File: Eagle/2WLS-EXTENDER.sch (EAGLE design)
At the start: 5 parts

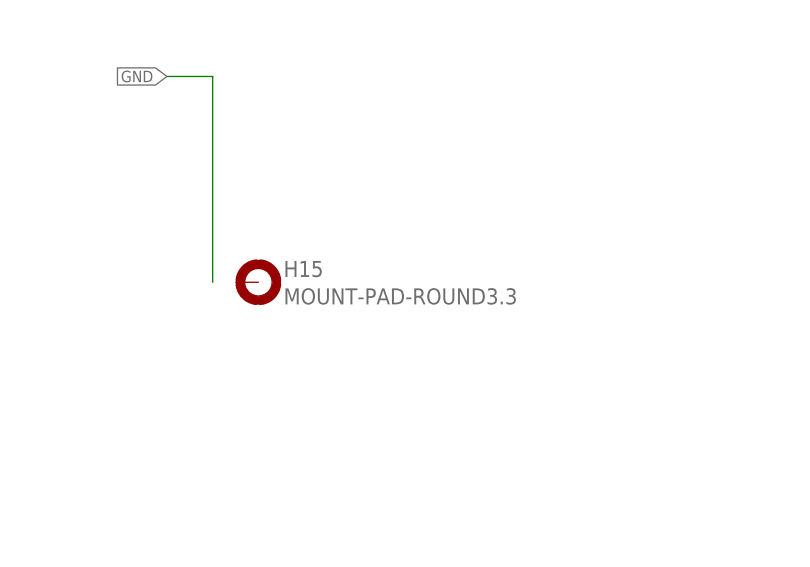
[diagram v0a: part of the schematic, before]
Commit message: Adjust dimensions to fit Keen case.
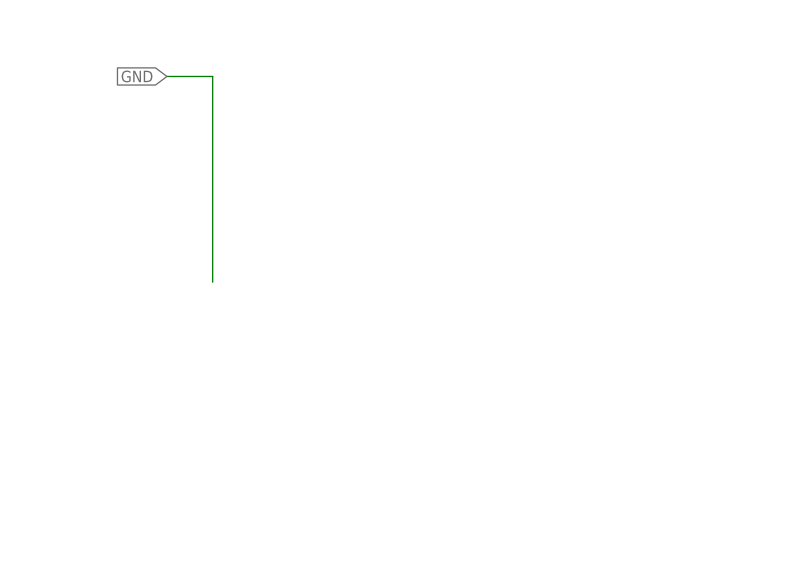
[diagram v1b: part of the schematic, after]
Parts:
- removed H15: MOUNT-PAD-ROUND3.3, holes:MOUNT-PAD-ROUND3.3
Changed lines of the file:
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@@
 <part name="H7" library="holes" deviceset="MOUNT-PAD-ROUND" device="3.3"/>
 <part name="H8" library="holes" deviceset="MOUNT-PAD-ROUND" device="3.3"/>
-<part name="H15" library="holes" deviceset="MOUNT-PAD-ROUND" device="3.3"/>
 <part name="H1" library="holes" deviceset="MOUNT-PAD-ROUND" device="3.3"/>
 <part name="H2" library="holes" deviceset="MOUNT-PAD-ROUND" device="3.3"/>
@@
 <instance part="H7" gate="G$1" x="208.28" y="71.12"/>
 <instance part="H8" gate="G$1" x="208.28" y="63.5"/>
-<instance part="H15" gate="G$1" x="274.32" y="93.98"/>
 <instance part="H1" gate="G$1" x="208.28" y="91.44"/>
 <instance part="H2" gate="G$1" x="208.28" y="83.82"/>
